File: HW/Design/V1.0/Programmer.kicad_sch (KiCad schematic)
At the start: 21 parts, among them J4 SIL04, Q5 SI2302, U5 AVRxxDU28

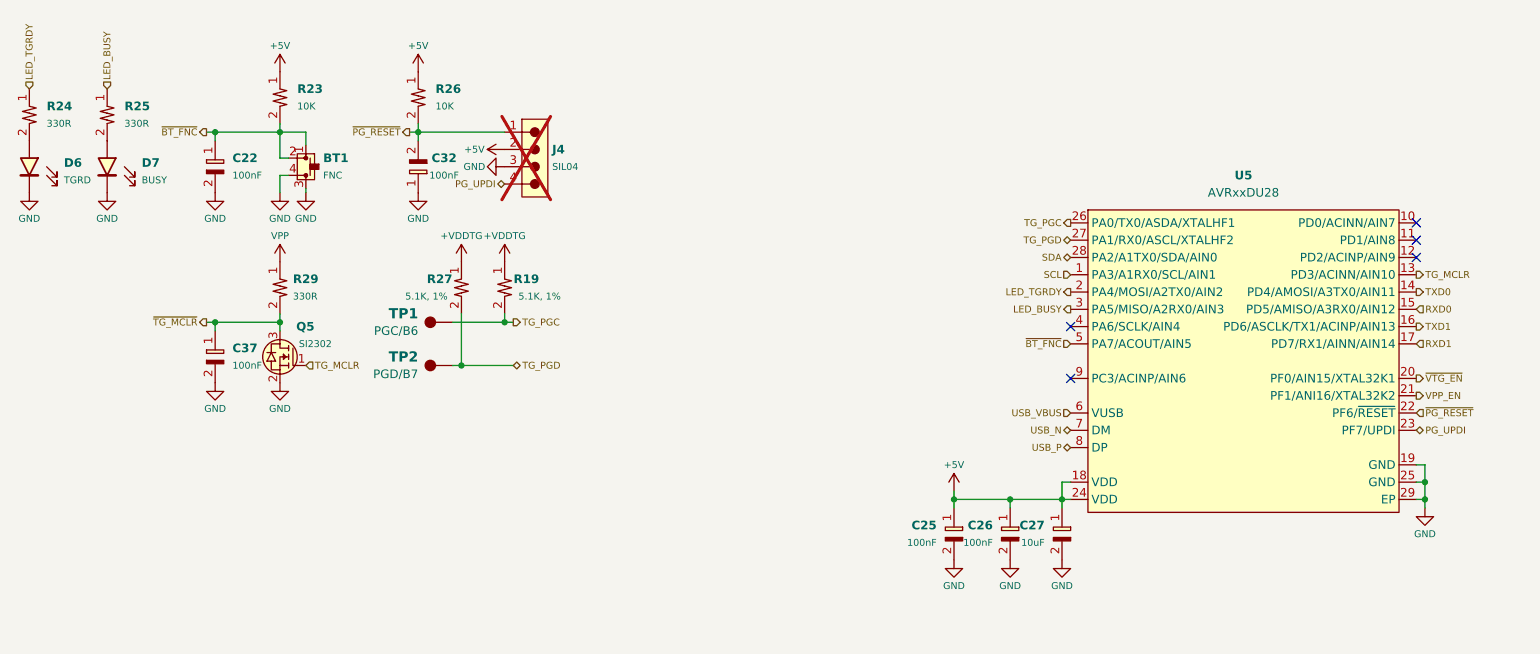
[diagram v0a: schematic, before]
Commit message: PCB V2: change programmer MCU
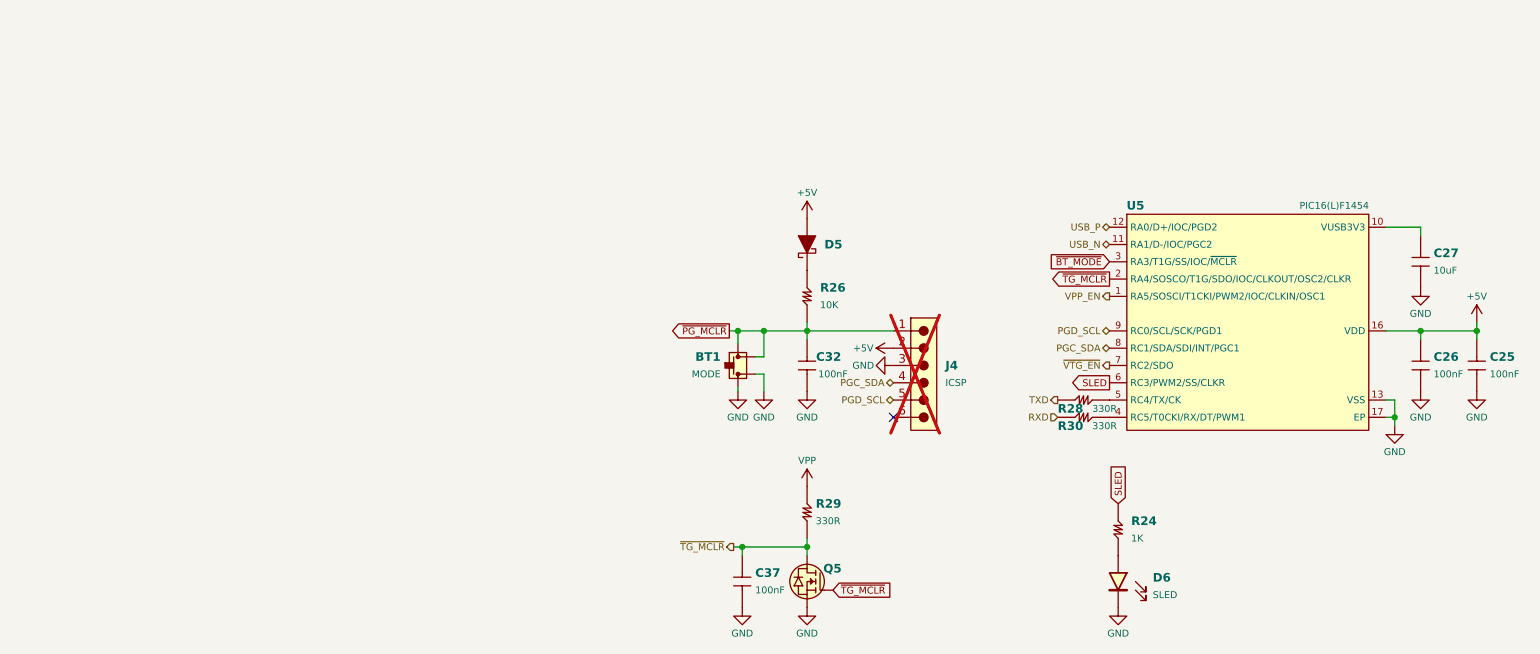
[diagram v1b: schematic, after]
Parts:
- removed C22: 100nF, SAMPI:CAP0603, symbol Triet_KiCAD_Sym:CAP_CER
- removed D7: BUSY, SAMPI:LED0603, symbol Triet_KiCAD_Sym:LED
- removed J4: SIL04, SAMPI:HD-1x4x1.27MM-TH, symbol SAMPI:SIL04-1
- removed R19, R27: 5.1K, 1%, SAMPI:RES0603, symbol Triet_KiCAD_Sym:RES
- removed R23: 10K, SAMPI:RES0603, symbol Triet_KiCAD_Sym:RES
- removed R25: 330R, SAMPI:RES0603, symbol Triet_KiCAD_Sym:RES
- removed TP1: PGC/B6, SAMPI:TP1MM, symbol SAMPI:TESTPOINT
- removed TP2: PGD/B7, SAMPI:TP1MM, symbol SAMPI:TESTPOINT
- removed U5: AVRxxDU28, SAMPI:VQFN28-4x4-EP, symbol SAMPI:AVRxxDU28
- added D5: 200mA/0.2VF, SAMPI:SOD-123FL, symbol SAMPI:BAT42
- added J4: ICSP, SAMPI:HD-1x6x1.27MM-TH, symbol SAMPI:SIL06
- added R28, R30: 330R, SAMPI:RES0603, symbol SAMPI:RES
- added U5: PIC16(L)F1454, SAMPI:VQFN16-P0.65-4x4, symbol SAMPI:PIC16(L)F1454
- BT1: value FNC -> MODE; footprint Liem:SW6x6-G -> SAMPI:SW6x6-G
- C25, C26, C27, C32, C37: symbol Triet_KiCAD_Sym:CAP_CER -> SAMPI:CERCAP
- D6: value TGRD -> SLED
- R24: value 330R -> 1K; symbol Triet_KiCAD_Sym:RES -> SAMPI:RES
- R26, R29: symbol Triet_KiCAD_Sym:RES -> SAMPI:RES
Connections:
- net LED_TGRDY is gone; now on an unnamed net: R24.1
- net TG_MCLR is gone; now on net ~{TG_MCLR}: Q5.1 (G)
- net +5V: now also C25.2, C26.2, D5.A, J4.2, U5.16 (VDD); no longer C25.1, C26.1, C27.1, R26.1
- net GND: now also C25.1, C26.1, C32.2, C37.1, J4.3, U5.13 (VSS), U5.17 (EP); no longer C25.2, C26.2, C32.1, C37.2
- net USB_N: now also U5.11 (RA1/D-/IOC/PGC2)
- net USB_P: now also U5.12 (RA0/D+/IOC/PGD2)
- net VPP_EN: now also U5.1 (RA5/SOSCI/T1CKI/PWM2/IOC/CLKIN/OSC1)
- net ~{TG_MCLR}: now also C37.2, U5.2 (RA4/SOSCO/T1G/SDO/IOC/CLKOUT/OSC2/CLKR); no longer C37.1
- net ~{VTG_EN}: now also U5.7 (RC2/SDO)
- net at D6.A: no longer R24.2
- net ~{BT_FNC} renamed ~{PG_MCLR}
- net ~{PG_MCLR}: now also C32.1, R26.1, J4.1
- net ~{PG_RESET}: no longer names the net of R26.2
- net ~{PG_RESET}: now also D5.K; no longer C32.2
- new net: C27.1, U5.10 (VUSB3V3)
- new net: R30.2, U5.4 (RC5/T0CKI/RX/DT/PWM1)
- new net: R28.2, U5.5 (RC4/TX/CK)
- new net PGC_SDA: J4.4, U5.8 (RC1/SDA/SDI/INT/PGC1)
- new net PGD_SCL: J4.5, U5.9 (RC0/SCL/SCK/PGD1)
- new net RXD: R30.1
- new net SLED: R24.2, U5.6 (RC3/PWM2/SS/CLKR)
- new net TXD: R28.1
- new net ~{BT_MODE}: U5.3 (RA3/T1G/SS/IOC/~{MCLR})
- no-connect marks 5 -> 1
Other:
- moved on the sheet: D6
